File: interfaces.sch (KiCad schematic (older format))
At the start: 86 parts, among them IC3 TPD8S009DSMR, J4 WE_629105150521, J6 685119134923, J7 1140084168, Q2 BSS138APW, Q3 BSS138APW, Q4 BSS138APW, Q5 BSS138APW, Q6 BSS138APW, U7 FT4232HQ, U8 SRST

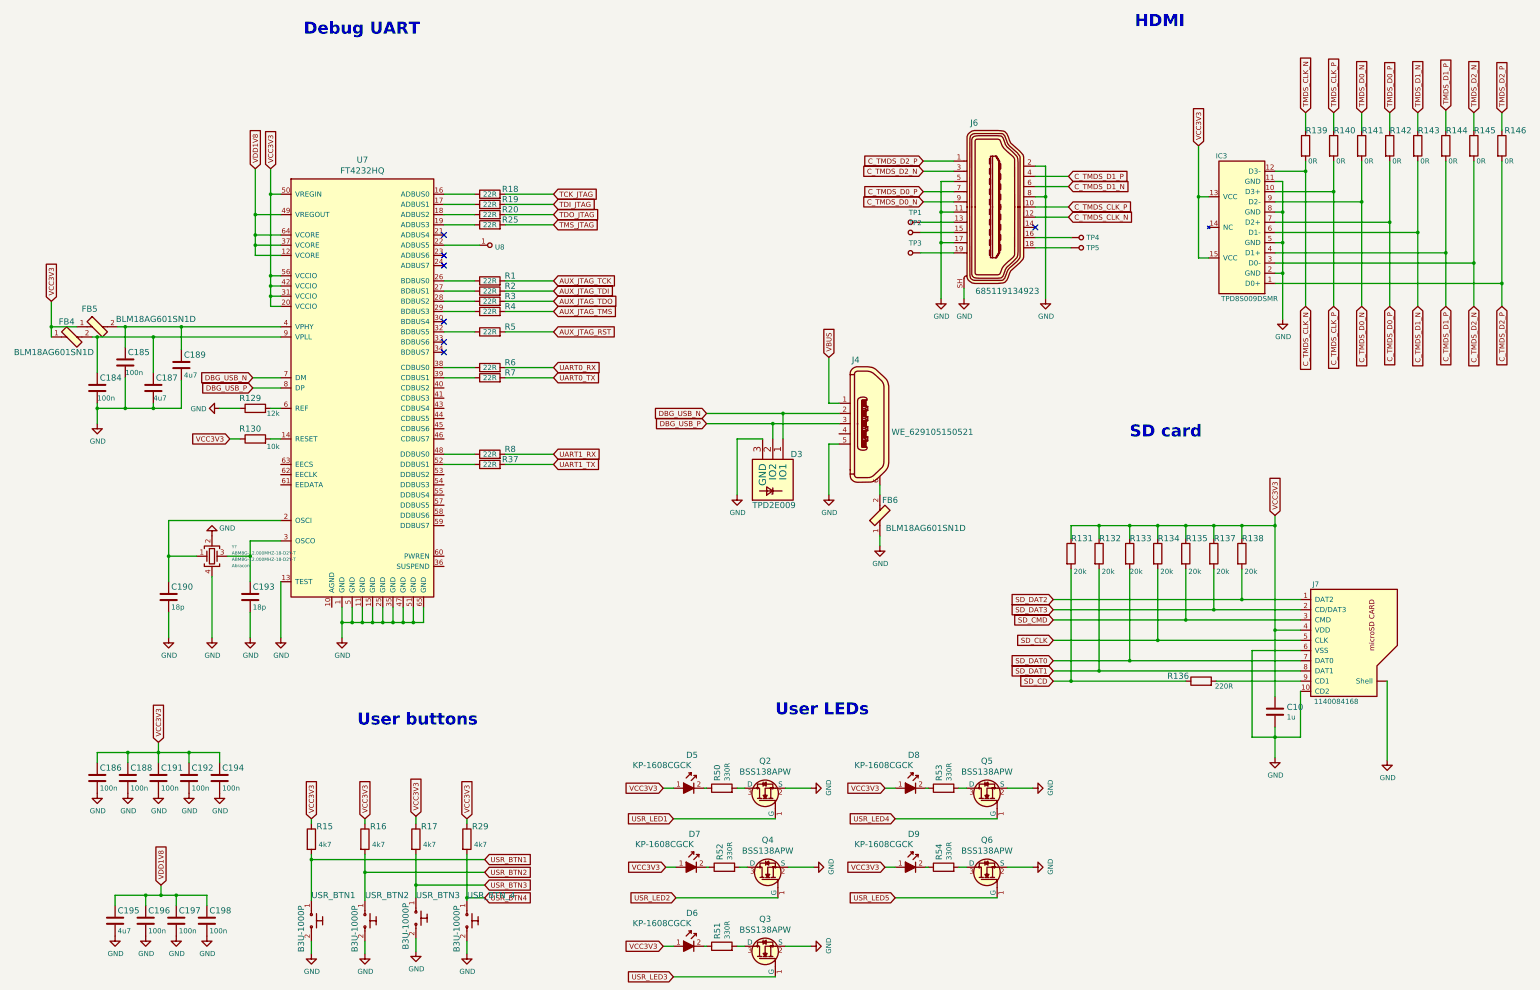
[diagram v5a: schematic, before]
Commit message: Replace VCC3V3 with 3V3_SYS
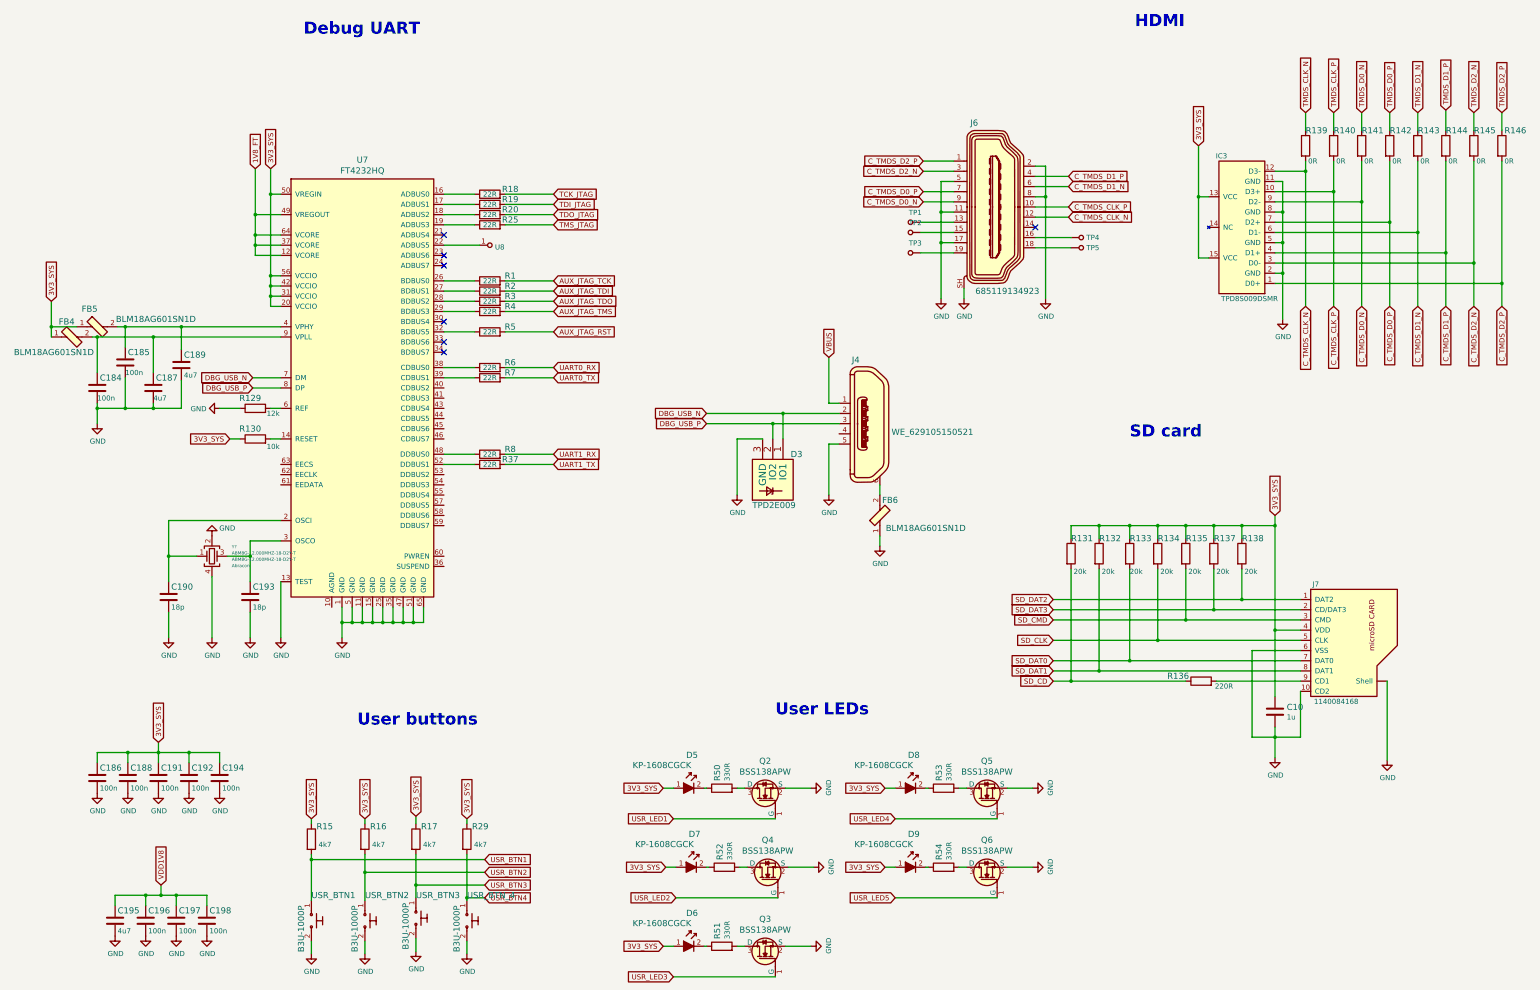
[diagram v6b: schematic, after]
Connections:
- net VDD1V8: no longer U7.12 (VCORE), U7.37 (VCORE), U7.49 (VREGOUT), U7.64 (VCORE)
- net VCC3V3 renamed 3V3_SYS
- new net 1V8_FT: U7.12 (VCORE), U7.37 (VCORE), U7.49 (VREGOUT), U7.64 (VCORE)
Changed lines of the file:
@@
 	8925 5050 8925 4600
 Text GLabel 2350 8375 1    50   Input ~ 0
-VCC3V3
+3V3_SYS
 $Comp
 L lpddr4-test-board:TPD2E009 D3
@@
 	2375 9875 2225 9875
 Text GLabel 3300 2750 1    50   Input ~ 0
-VDD1V8
+1V8_FT
 Text GLabel 3450 2750 1    50   Input ~ 0
-VCC3V3
+3V3_SYS
 Text GLabel 1300 4050 1    50   Input ~ 0
-VCC3V3
+3V3_SYS
 Wire Wire Line
 	1300 4050 1300 4300
@@
 	1300 4300 1300 4400
 Text GLabel 3050 5400 0    50   Input ~ 0
-VCC3V3
+3V3_SYS
 Text GLabel 8925 4600 1    50   Input ~ 0
 VBUS
@@
 	12550 3025 12550 2525
 Text GLabel 12550 2525 1    50   Input ~ 0
-VCC3V3
+3V3_SYS
 $Comp
 L lpddr4-test-board:1140084168 J7
@@
 	12700 6375 12700 6250
 Text GLabel 13300 6150 1    50   Input ~ 0
-VCC3V3
+3V3_SYS
 Text Notes 3775 1450 0    118  ~ 24
 Debug UART
@@
 	7700 8825 7725 8825
 Text GLabel 7300 8825 0    50   Input ~ 0
-VCC3V3
+3V3_SYS
 Wire Wire Line
 	7300 8825 7400 8825
@@
 	7725 9600 7750 9600
 Text GLabel 7325 9600 0    50   Input ~ 0
-VCC3V3
+3V3_SYS
 Wire Wire Line
 	7325 9600 7425 9600
@@
 	9875 8825 9900 8825
 Text GLabel 9475 8825 0    50   Input ~ 0
-VCC3V3
+3V3_SYS
 Wire Wire Line
 	9475 8825 9575 8825
@@
 	9875 9600 9900 9600
 Text GLabel 9475 9600 0    50   Input ~ 0
-VCC3V3
+3V3_SYS
 Wire Wire Line
 	9475 9600 9575 9600
@@
 	7700 10375 7725 10375
 Text GLabel 7300 10375 0    50   Input ~ 0
-VCC3V3
+3V3_SYS
 Wire Wire Line
 	7300 10375 7400 10375
@@
 VDD1V8
 Text GLabel 3850 9125 1    50   Input ~ 0
-VCC3V3
+3V3_SYS
 Text GLabel 4375 9125 1    50   Input ~ 0
-VCC3V3
+3V3_SYS
 Text GLabel 4875 9100 1    50   Input ~ 0
-VCC3V3
+3V3_SYS
 Text GLabel 5375 9125 1    50   Input ~ 0
-VCC3V3
+3V3_SYS
 $Comp
 L antmicroCrystals:ABM8G-12.000MHZ-18-D2Y-T Y?

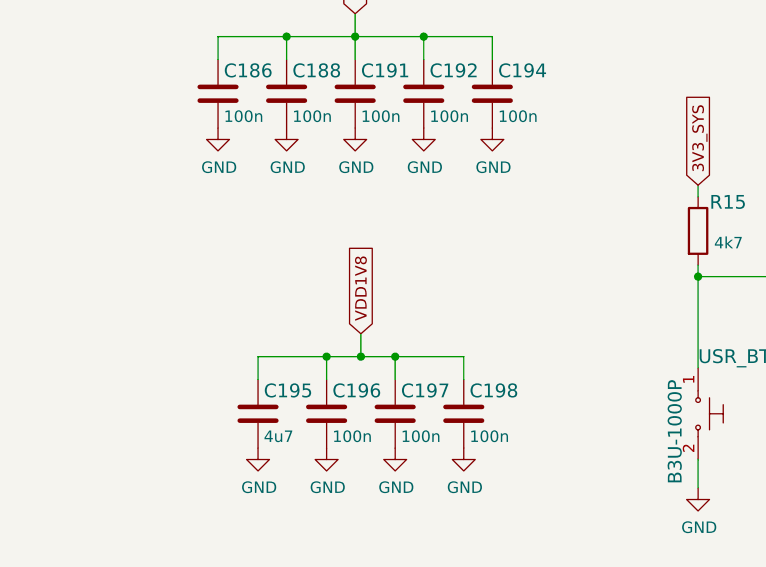
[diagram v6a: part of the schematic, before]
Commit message: Introduce unified 1V1_SYS 1V8_SYS 3V3_SYS
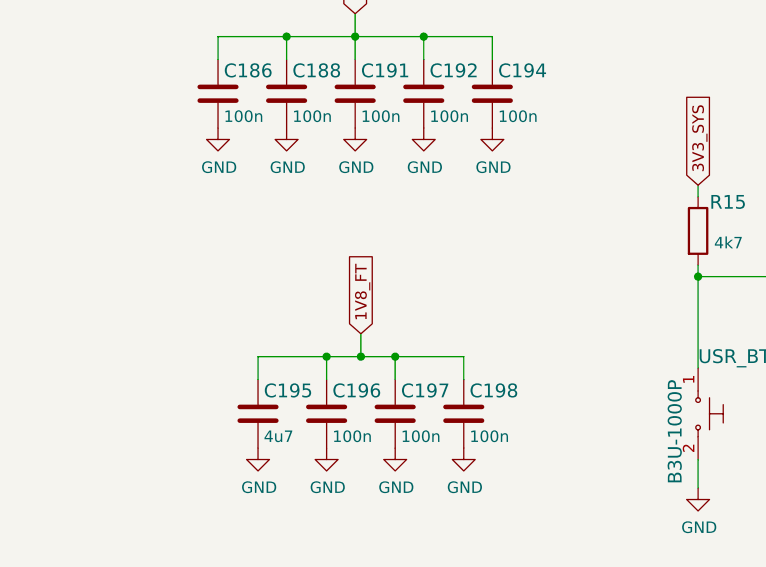
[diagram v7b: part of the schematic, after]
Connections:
- net VDD1V8 is gone; now on net 1V8_FT: C195.1, C196.1, C197.1, C198.1
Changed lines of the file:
@@
 NoConn ~ 5150 4550
 Text GLabel 2375 9775 1    50   Input ~ 0
-VDD1V8
+1V8_FT
 Text GLabel 3850 9125 1    50   Input ~ 0
 3V3_SYS

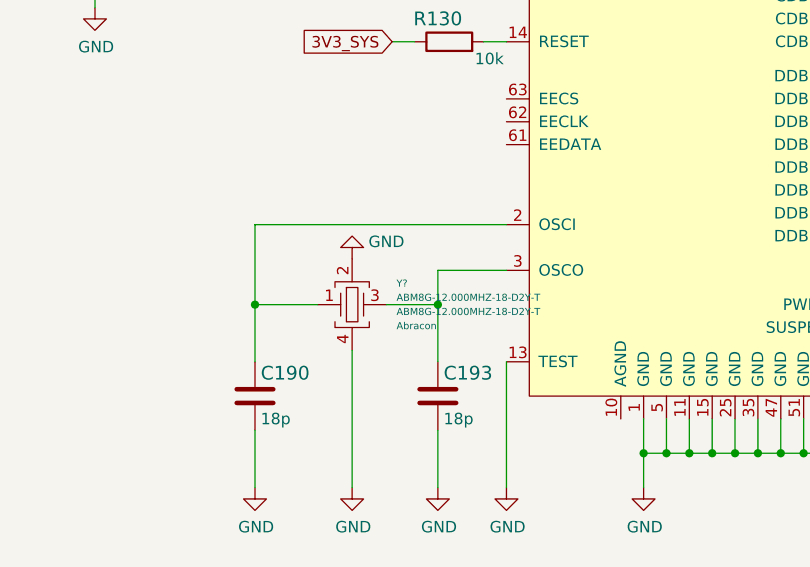
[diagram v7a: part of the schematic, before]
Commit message: Make Supply more compact
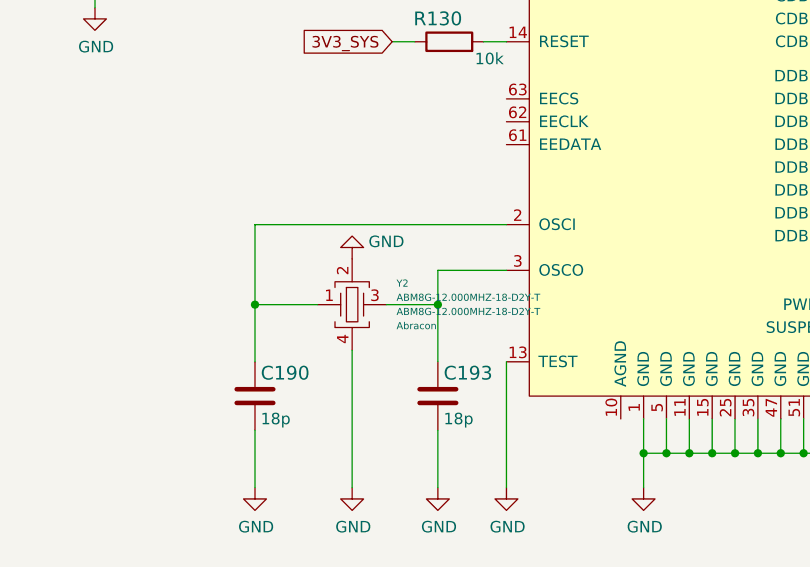
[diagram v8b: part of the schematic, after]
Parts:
- gave numbers to parts that had none: 1
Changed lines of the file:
@@
 3V3_SYS
 $Comp
-L antmicroCrystals:ABM8G-12.000MHZ-18-D2Y-T Y?
+L antmicroCrystals:ABM8G-12.000MHZ-18-D2Y-T Y2
 U 1 1 61D2EA50
 P 2875 6550
-F 0 "Y?" H 3069 6643 31  0000 L CNN
+F 0 "Y2" H 3069 6643 31  0000 L CNN
 F 1 "ABM8G-12.000MHZ-18-D2Y-T" H 3069 6581 31  0000 L CNN
 F 2 "antmicro-footprints:KX-7" H 4975 6550 50  0001 C CNN
@@
 	2875 6750 2875 7350
 $Comp
-L lpddr4-test-board:GND #PWR?
+L lpddr4-test-board:GND #PWR0137
 U 1 1 61E026BC
 P 2875 7350
-F 0 "#PWR?" H 2875 7100 50  0001 C CNN
+F 0 "#PWR0137" H 2875 7100 50  0001 C CNN
 F 1 "GND" H 2880 7177 50  0000 C CNN
 F 2 "" H 2875 7350 50  0001 C CNN
@@
 $EndComp
 $Comp
-L lpddr4-test-board:GND #PWR?
+L lpddr4-test-board:GND #PWR0138
 U 1 1 61E1A1A0
 P 2875 6350
-F 0 "#PWR?" H 2875 6100 50  0001 C CNN
+F 0 "#PWR0138" H 2875 6100 50  0001 C CNN
 F 1 "GND" H 2725 6275 50  0000 C CNN
 F 2 "" H 2875 6350 50  0001 C CNN
